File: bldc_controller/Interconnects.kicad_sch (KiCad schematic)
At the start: 45 parts, among them J10 Conn_01x06, J3 Conn_01x02, J4 Conn_01x07, J5 Conn_01x08, J6 SWD_02x05_1.27mm, J7 Conn_01x03, J8 Conn_01x03, J9 Conn_01x02, SW1 CAS-220TA

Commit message: some progress
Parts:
- removed D1, D2: BAT41KFILM, symbol Device:D_Schottky
- added D9 (x2): BAT41KFILM, Diode_SMD:D_SOD-523, symbol 0_diode:BAT41KFILM
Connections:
- net AUX2_B_K: now also D9.1 (K)
- net AUX2_C_K: now also D9.1 (K)
- net AUX2_I2C_PULLUP: now also D9.2 (A), D9.2 (A)
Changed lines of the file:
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@@
-    )
-  )
-  (symbol (lib_id "Device:D_Schottky") (at 76.2 111.76 90) (unit 1)
-    (in_bom yes) (on_board yes) (dnp no)
-    (property "Reference" "D1" (at 78.105 110.49 90)
-      (effects (font (size 1.27 1.27)) (justify right))
-    )
-    (property "Value" "BAT41KFILM" (at 78.105 113.03 90)
-      (effects (font (size 1.27 1.27)) (justify right))
-    )
-    (property "Footprint" "" (at 76.2 111.76 0)
-      (effects (font (size 1.27 1.27)) hide)
-    )
-    (property "Datasheet" "~" (at 76.2 111.76 0)
-      (effects (font (size 1.27 1.27)) hide)
-    )
-    (pin "1")
-    (pin "2")
-    (instances
-      (project "bldc_controller"
-        (path "/0650c7a8-acba-429c-9f8e-eec0baf0bc1c/e3d7d553-09c9-41e5-aeb8-81d1255a4873"
-          (reference "D1") (unit 1)
-        )
-      )
     )
   )
@@
     )
   )
+  (symbol (lib_id "0_diode:BAT41KFILM") (at 76.2 111.76 90) (unit 1)
+    (in_bom yes) (on_board yes) (dnp no)
+    (property "Reference" "D9" (at 78.105 110.49 90)
+      (effects (font (size 1.27 1.27)) (justify right))
+    )
+    (property "Value" "BAT41KFILM" (at 78.105 113.03 90)
+      (effects (font (size 1.27 1.27)) (justify right))
+    )
+    (property "Footprint" "Diode_SMD:D_SOD-523" (at 80.645 111.76 0)
+      (effects (font (size 1.27 1.27)) hide)
+    )
+    (property "Datasheet" "https://www.mouser.ch/datasheet/2/389/bat41-1848934.pdf" (at 76.2 111.76 0)
+      (effects (font (size 1.27 1.27)) hide)
+    )
+    (pin "1")
+    (pin "2")
+    (instances
+      (project "bldc_controller"
+        (path "/0650c7a8-acba-429c-9f8e-eec0baf0bc1c/a6223e2e-2896-4182-b4ad-55a63bc87f3d"
+          (reference "D9") (unit 1)
+        )
+        (path "/0650c7a8-acba-429c-9f8e-eec0baf0bc1c/e3d7d553-09c9-41e5-aeb8-81d1255a4873"
+          (reference "D1") (unit 1)
+        )
+      )
+    )
+  )
   (symbol (lib_id "power:+3V3") (at 57.15 105.41 0) (unit 1)
     (in_bom yes) (on_board yes) (dnp no) (fields_autoplaced)
@@
         (path "/0650c7a8-acba-429c-9f8e-eec0baf0bc1c/e3d7d553-09c9-41e5-aeb8-81d1255a4873"
           (reference "#PWR034") (unit 1)
+        )
+      )
+    )
+  )
+  (symbol (lib_id "0_diode:BAT41KFILM") (at 91.44 111.76 90) (unit 1)
+    (in_bom yes) (on_board yes) (dnp no)
+    (property "Reference" "D9" (at 93.345 110.49 90)
+      (effects (font (size 1.27 1.27)) (justify right))
+    )
+    (property "Value" "BAT41KFILM" (at 93.345 113.03 90)
+      (effects (font (size 1.27 1.27)) (justify right))
+    )
+    (property "Footprint" "Diode_SMD:D_SOD-523" (at 95.885 111.76 0)
+      (effects (font (size 1.27 1.27)) hide)
+    )
+    (property "Datasheet" "https://www.mouser.ch/datasheet/2/389/bat41-1848934.pdf" (at 91.44 111.76 0)
+      (effects (font (size 1.27 1.27)) hide)
+    )
+    (pin "1")
+    (pin "2")
+    (instances
+      (project "bldc_controller"
+        (path "/0650c7a8-acba-429c-9f8e-eec0baf0bc1c/a6223e2e-2896-4182-b4ad-55a63bc87f3d"
+          (reference "D9") (unit 1)
+        )
+        (path "/0650c7a8-acba-429c-9f8e-eec0baf0bc1c/e3d7d553-09c9-41e5-aeb8-81d1255a4873"
+          (reference "D2") (unit 1)
         )
       )
@@
         )
       )
-    )
-  )
-  (symbol (lib_id "Device:D_Schottky") (at 91.44 111.76 90) (unit 1)
-    (in_bom yes) (on_board yes) (dnp no)
-    (property "Reference" "D2" (at 93.345 110.49 90)
-      (effects (font (size 1.27 1.27)) (justify right))
-    )
-    (property "Value" "BAT41KFILM" (at 93.345 113.03 90)
-      (effects (font (size 1.27 1.27)) (justify right))
-    )
-    (property "Footprint" "" (at 91.44 111.76 0)
-      (effects (font (size 1.27 1.27)) hide)
-    )
-    (property "Datasheet" "~" (at 91.44 111.76 0)
-      (effects (font (size 1.27 1.27)) hide)
-    )
-    (pin "1")
-    (pin "2")
-    (instances
-      (project "bldc_controller"
-        (path "/0650c7a8-acba-429c-9f8e-eec0baf0bc1c/e3d7d553-09c9-41e5-aeb8-81d1255a4873"
-          (reference "D2") (unit 1)
-        )
-      )

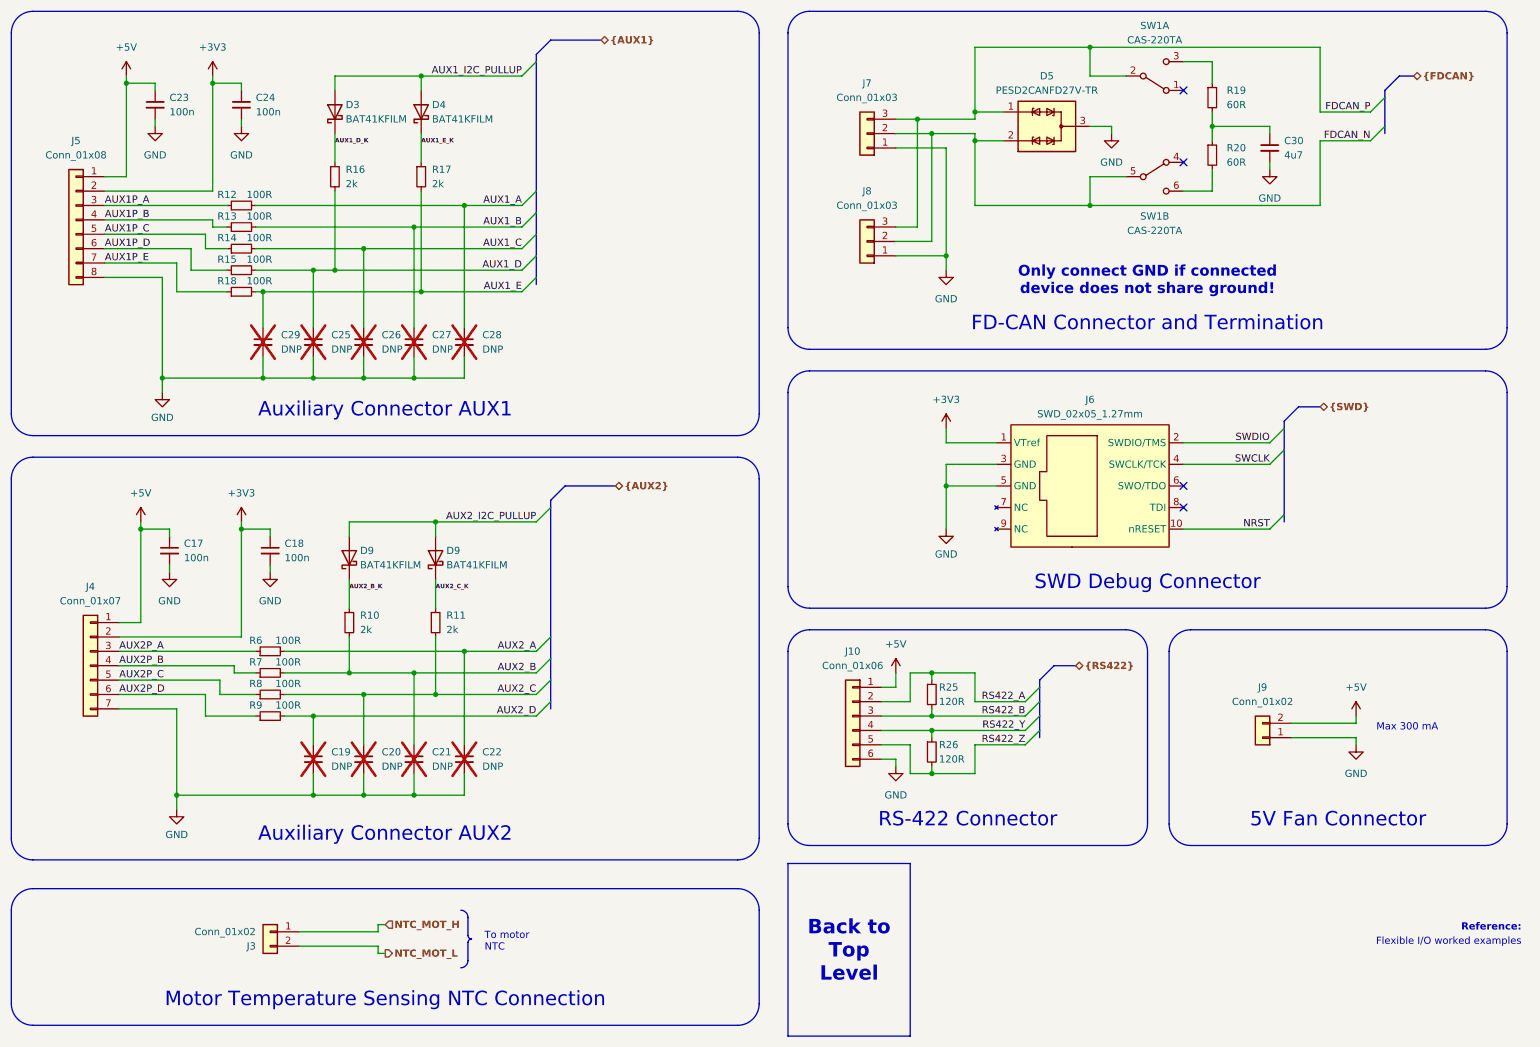
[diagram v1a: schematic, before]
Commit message: added temporary footprints and deleted extra files
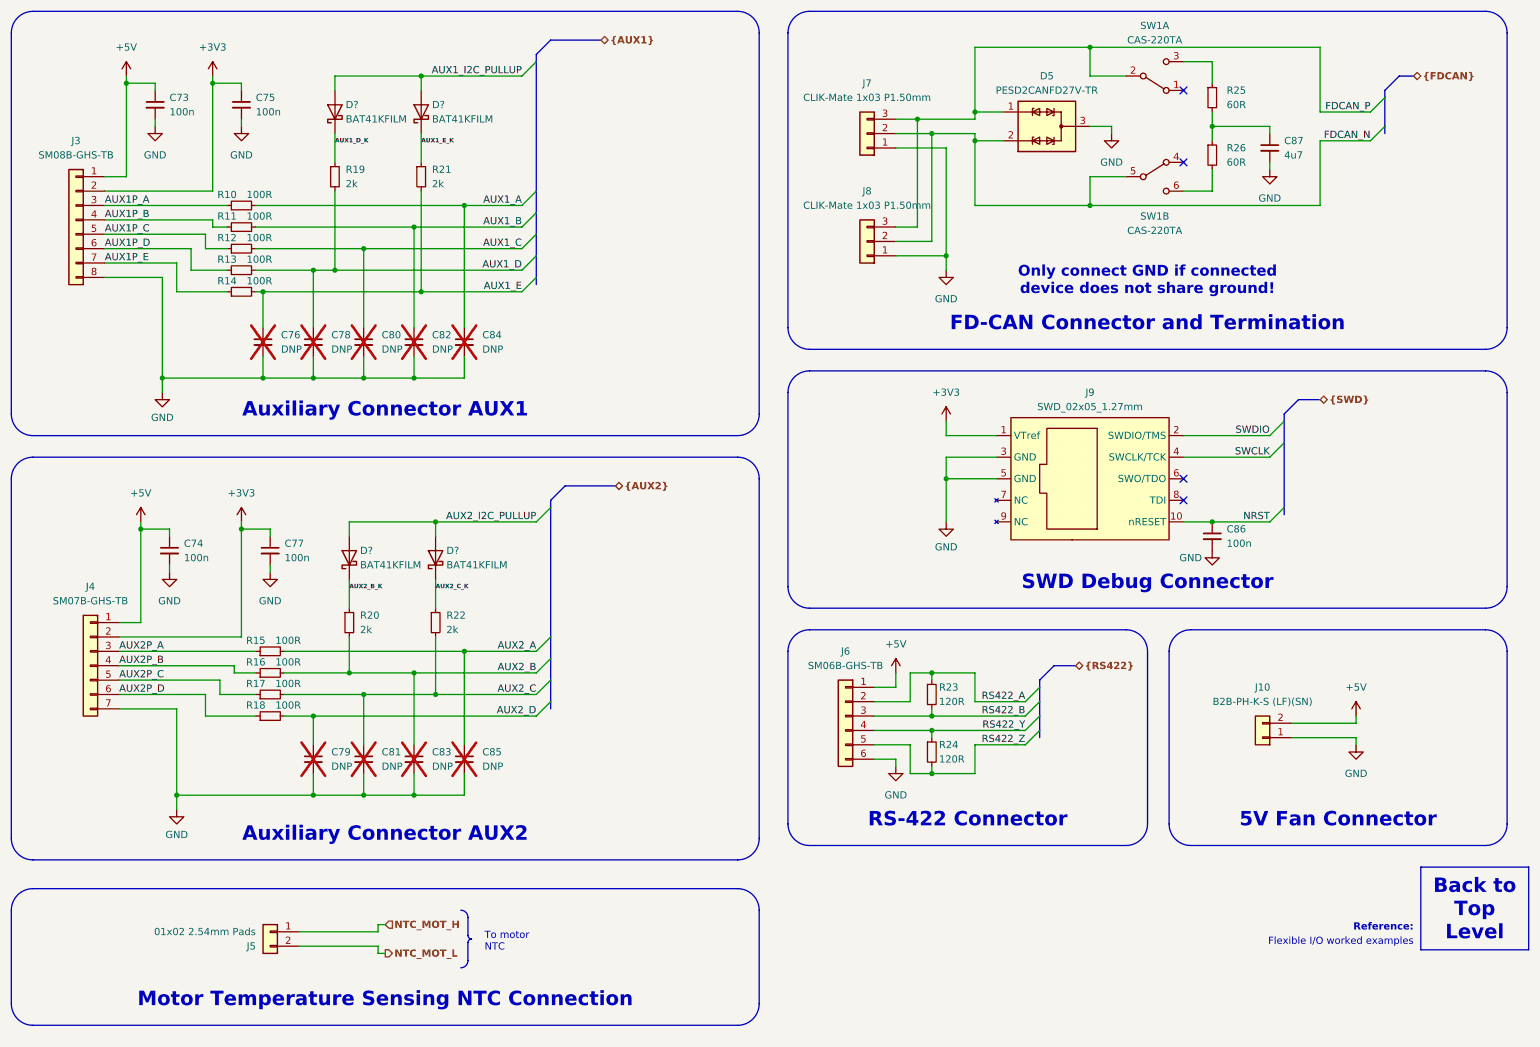
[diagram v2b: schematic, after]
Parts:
- removed D3, D4: BAT41KFILM, symbol Device:D_Schottky
- removed D9 (x2): BAT41KFILM, Diode_SMD:D_SOD-523, symbol 0_diode:BAT41KFILM
- added C86: 100n, Capacitor_SMD:C_0402_1005Metric, symbol Device:C_Small
- added D? (x4): BAT41KFILM, Diode_SMD:D_SOD-523, symbol 0_diode:BAT41KFILM
- C73: renamed from C23; footprint (none) -> Capacitor_SMD:C_0402_1005Metric
- C74: renamed from C17; footprint (none) -> Capacitor_SMD:C_0402_1005Metric
- C75: renamed from C24; footprint (none) -> Capacitor_SMD:C_0402_1005Metric
- C76: renamed from C29; footprint (none) -> Capacitor_SMD:C_0402_1005Metric
- C77: renamed from C18; footprint (none) -> Capacitor_SMD:C_0402_1005Metric
- C78: renamed from C25; footprint (none) -> Capacitor_SMD:C_0402_1005Metric
- C79: renamed from C19; footprint (none) -> Capacitor_SMD:C_0402_1005Metric
- C80: renamed from C26; footprint (none) -> Capacitor_SMD:C_0402_1005Metric
- C81: renamed from C20; footprint (none) -> Capacitor_SMD:C_0402_1005Metric
- C82: renamed from C27; footprint (none) -> Capacitor_SMD:C_0402_1005Metric
- C83: renamed from C21; footprint (none) -> Capacitor_SMD:C_0402_1005Metric
- C84: renamed from C28; footprint (none) -> Capacitor_SMD:C_0402_1005Metric
- C85: renamed from C22; footprint (none) -> Capacitor_SMD:C_0402_1005Metric
- C87: renamed from C30; footprint (none) -> Capacitor_SMD:C_0603_1608Metric
- J10: renamed from J9; value Conn_01x02 -> B2B-PH-K-S (LF)(SN); footprint (none) -> Connector_JST:JST_PH_B2B-PH-K_1x02_P2.00mm_Vertical
- J3: renamed from J5; value Conn_01x08 -> SM08B-GHS-TB; footprint (none) -> Connector_JST:JST_GH_SM08B-GHS-TB_1x08-1MP_P1.25mm_Horizontal
- J4: value Conn_01x07 -> SM07B-GHS-TB; footprint (none) -> Connector_JST:JST_GH_SM07B-GHS-TB_1x07-1MP_P1.25mm_Horizontal
- J5: renamed from J3; value Conn_01x02 -> 01x02 2.54mm Pads; footprint (none) -> Connector_PinHeader_2.54mm:PinHeader_1x02_P2.54mm_Vertical
- J6: renamed from J10; value Conn_01x06 -> SM06B-GHS-TB; footprint (none) -> Connector_JST:JST_GH_SM06B-GHS-TB_1x06-1MP_P1.25mm_Horizontal
- J7, J8: value Conn_01x03 -> CLIK-Mate 1x03 P1.50mm; footprint (none) -> Connector_Molex:Molex_CLIK-Mate_502585-0370_1x03-1MP_P1.50mm_Horizontal
- R10: renamed from R12; footprint (none) -> Resistor_SMD:R_0402_1005Metric
- R11: renamed from R13; footprint (none) -> Resistor_SMD:R_0402_1005Metric
- R12: renamed from R14; footprint (none) -> Resistor_SMD:R_0402_1005Metric
- R13: renamed from R15; footprint (none) -> Resistor_SMD:R_0402_1005Metric
- R14: renamed from R18; footprint (none) -> Resistor_SMD:R_0402_1005Metric
- R15: renamed from R6; footprint (none) -> Resistor_SMD:R_0402_1005Metric
- R16: renamed from R7; footprint (none) -> Resistor_SMD:R_0402_1005Metric
- R17: renamed from R8; footprint (none) -> Resistor_SMD:R_0402_1005Metric
- R18: renamed from R9; footprint (none) -> Resistor_SMD:R_0402_1005Metric
- R19: renamed from R16; footprint (none) -> Resistor_SMD:R_0402_1005Metric
- R20: renamed from R10; footprint (none) -> Resistor_SMD:R_0402_1005Metric
- R21: renamed from R17; footprint (none) -> Resistor_SMD:R_0402_1005Metric
- R22: renamed from R11; footprint (none) -> Resistor_SMD:R_0402_1005Metric
- R23: renamed from R25; footprint (none) -> Resistor_SMD:R_0402_1005Metric
- R24: renamed from R26; footprint (none) -> Resistor_SMD:R_0402_1005Metric
- R25: renamed from R19; footprint (none) -> Resistor_SMD:R_0603_1608Metric
- R26: renamed from R20; footprint (none) -> Resistor_SMD:R_0603_1608Metric
- renumbered J6 to J9
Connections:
- net AUX1_D_K: now also D?.1 (K)
- net AUX1_E_K: now also D?.1 (K)
- net AUX1_I2C_PULLUP: now also D?.2 (A), D?.2 (A)
- net AUX2_B_K: now also D?.1 (K)
- net AUX2_C_K: now also D?.1 (K)
- net AUX2_I2C_PULLUP: now also D?.2 (A), D?.2 (A)
- net GND: now also C86.2
- net NRST: now also C86.1
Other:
- moved on the sheet: J6, J9

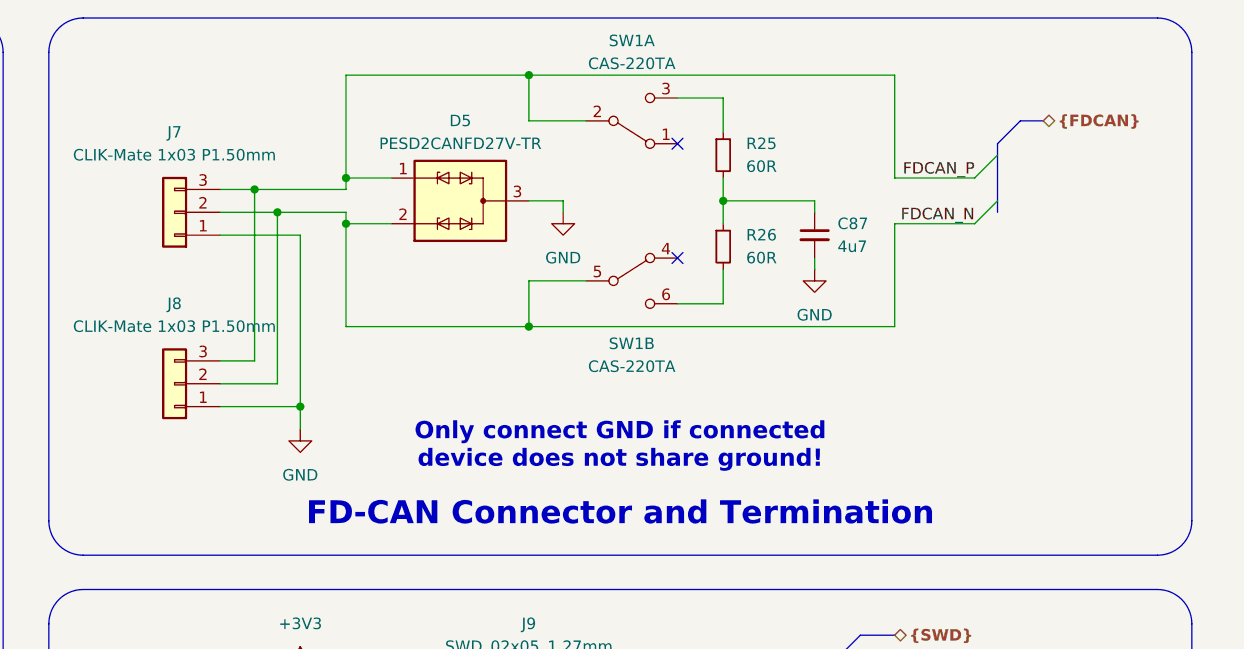
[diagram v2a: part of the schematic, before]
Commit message: added IPC-7351 compliant footprints and started routing
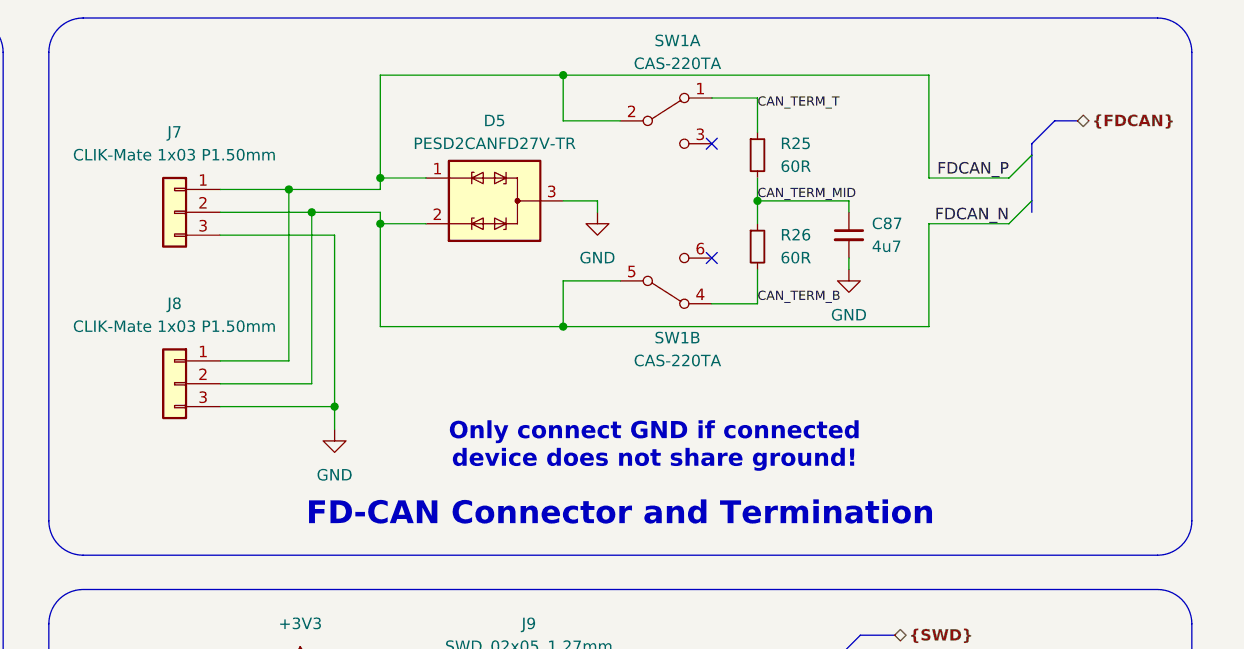
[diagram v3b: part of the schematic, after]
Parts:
- C73, C74, C75, C76, C77, C78, C79, C80, C81, C82, C83, C84, C85, C86: footprint Capacitor_SMD:C_0402_1005Metric -> 0_capacitor_smd:C_0402_1005_DensityHigh
- C87: footprint Capacitor_SMD:C_0603_1608Metric -> 0_capacitor_smd:C_0603_1608_DensityHigh
- R10, R11, R12, R13, R14, R15, R16, R17, R18, R19, R20, R21, R22, R23, R24: footprint Resistor_SMD:R_0402_1005Metric -> 0_resistor_smd:R_0402_1005_DensityHigh
- R25, R26: footprint Resistor_SMD:R_0603_1608Metric -> 0_resistor_smd:R_0603_1608_DensityHigh
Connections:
- net FDCAN_P: now also J7.1 (Pin_1), J8.1 (Pin_1); no longer J7.3 (Pin_3), J8.3 (Pin_3)
- net GND: now also J7.3 (Pin_3), J8.3 (Pin_3); no longer J7.1 (Pin_1), J8.1 (Pin_1)
- net CAN_TERM_MID: now reaches C87.1, R25.2, R26.1
- net at SW1.6 (C): no longer R26.2
- net at SW1.3 (C): no longer R25.1
- net CAN_TERM_T: now reaches SW1.1 (A)
- net CAN_TERM_T: now also R25.1
- net CAN_TERM_B: now reaches SW1.4 (A)
- net CAN_TERM_B: now also R26.2
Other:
- moved on the sheet: C87, D5, J7, J8, R25, R26, SW1A, SW1B

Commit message: some progress on the pcb
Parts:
- J7, J8: value CLIK-Mate 1x03 P1.50mm -> Microfit 3.0 1x03; footprint Connector_Molex:Molex_CLIK-Mate_502585-0370_1x03-1MP_P1.50mm_Horizontal -> Connector_Molex:Molex_Micro-Fit_3.0_43650-0310_1x03-1MP_P3.00mm_Horizontal
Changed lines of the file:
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@@
-    )
-  )
-  (symbol (lib_id "Connector_Generic:Conn_01x03") (at 167.64 55.88 0) (mirror y) (unit 1)
-    (in_bom yes) (on_board yes) (dnp no)
-    (property "Reference" "J8" (at 167.64 46.99 0)
-      (effects (font (size 1.27 1.27)))
-    )
-    (property "Value" "CLIK-Mate 1x03 P1.50mm" (at 167.64 49.53 0)
-      (effects (font (size 1.27 1.27)))
-    )
-    (property "Footprint" "Connector_Molex:Molex_CLIK-Mate_502585-0370_1x03-1MP_P1.50mm_Horizontal" (at 167.64 55.88 0)
-      (effects (font (size 1.27 1.27)) hide)
-    )
-    (property "Datasheet" "~" (at 167.64 55.88 0)
-      (effects (font (size 1.27 1.27)) hide)
-    )
-    (pin "1")
-    (pin "2")
-    (pin "3")
-    (instances
-      (project "bldc_controller"
-        (path "/0650c7a8-acba-429c-9f8e-eec0baf0bc1c/e3d7d553-09c9-41e5-aeb8-81d1255a4873"
-          (reference "J8") (unit 1)
-        )
-      )
     )
   )
@@
       (effects (font (size 1.27 1.27)))
     )
-    (property "Value" "CLIK-Mate 1x03 P1.50mm" (at 167.64 30.48 0)
-      (effects (font (size 1.27 1.27)))
-    )
-    (property "Footprint" "Connector_Molex:Molex_CLIK-Mate_502585-0370_1x03-1MP_P1.50mm_Horizontal" (at 167.64 36.83 0)
+    (property "Value" "Microfit 3.0 1x03" (at 167.64 30.48 0)
+      (effects (font (size 1.27 1.27)))
+    )
+    (property "Footprint" "Connector_Molex:Molex_Micro-Fit_3.0_43650-0310_1x03-1MP_P3.00mm_Horizontal" (at 167.64 36.83 0)
       (effects (font (size 1.27 1.27)) hide)
     )
@@
         )
       )
+    )
+  )
+  (symbol (lib_id "Connector_Generic:Conn_01x03") (at 167.64 55.88 0) (mirror y) (unit 1)
+    (in_bom yes) (on_board yes) (dnp no)
+    (property "Reference" "J8" (at 167.64 46.99 0)
+      (effects (font (size 1.27 1.27)))
+    )
+    (property "Value" "Microfit 3.0 1x03" (at 167.64 49.53 0)
+      (effects (font (size 1.27 1.27)))
+    )
+    (property "Footprint" "Connector_Molex:Molex_Micro-Fit_3.0_43650-0310_1x03-1MP_P3.00mm_Horizontal" (at 167.64 55.88 0)
+      (effects (font (size 1.27 1.27)) hide)
+    )
+    (property "Datasheet" "~" (at 167.64 55.88 0)
+      (effects (font (size 1.27 1.27)) hide)
+    )
+    (pin "1")
+    (pin "2")
+    (pin "3")
+    (instances
+      (project "bldc_controller"
+        (path "/0650c7a8-acba-429c-9f8e-eec0baf0bc1c/e3d7d553-09c9-41e5-aeb8-81d1255a4873"
+          (reference "J8") (unit 1)
+        )
+      )
